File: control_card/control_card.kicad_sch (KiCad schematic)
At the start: 1 part, among them J1 Conn_02x04_Counter_Clockwise

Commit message: Control Card Started : Schematic & PCB
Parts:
- added C1, C5, C7: 0.1µF, Capacitor_SMD:C_0402_1005Metric, symbol Device:C_Small
- added C10, C11, C12, C13, C20, C3, C4, C6, C9: 1µF, Capacitor_SMD:C_0402_1005Metric, symbol Device:C_Small
- added C14: 18pF, Capacitor_SMD:C_0402_1005Metric, symbol Device:C_Small
- added C15: 2.7pF, Capacitor_SMD:C_0402_1005Metric, symbol Device:C_Small
- added C16: 220pF, Capacitor_SMD:C_0402_1005Metric, symbol Device:C_Small
- added C17: 2pF, Capacitor_SMD:C_0402_1005Metric, symbol Device:C_Small
- added C18: 0.5pF, Capacitor_SMD:C_0402_1005Metric, symbol Device:C_Small
- added C19: 1pF, Capacitor_SMD:C_0402_1005Metric, symbol Device:C_Small
- added C2: 10µF, Capacitor_SMD:C_0402_1005Metric, symbol Device:C_Small
- added C8: 2.2µF, Capacitor_SMD:C_0402_1005Metric, symbol Device:C_Small
- added IC1: TLSR8253F512ET48, Package_DFN_QFN:QFN-48-1EP_7x7mm_P0.5mm_EP5.6x5.6mm_ThermalVias, symbol Library:TLSR8253F512ET48
- added L1: 47µH, Inductor_SMD:L_0805_2012Metric, symbol Device:L_Small
- added L2: 1.3nH, Inductor_SMD:L_0402_1005Metric, symbol Device:L_Small
- added L3: 3.3nF, Inductor_SMD:L_0402_1005Metric, symbol Device:L_Small
- added U1: Wifi, Footprint_Rang_Dong:Wifi CBU, symbol Library:Wifi_CBU
- added Y1: Crystal_GND24_Small, Footprint_Rang_Dong:Crystal_SMD_3225, symbol Device:Crystal_GND24_Small
- J1: footprint Connector_PinSocket_2.54mm:PinSocket_2x04_P2.54mm_Vertical -> Connector_PinHeader_2.54mm:PinHeader_2x04_P2.54mm_Vertical
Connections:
- net +3.3V: now also C1.1, C10.1, C13.1, C2.1, C9.1, IC1.15 (VDD_IO), IC1.26 (VDD3), IC1.27 (VDDIO_AMS), U1.14 (3V3), U1.18 (CEN)
- net CT1: now also U1.10 (P6), U1.11 (P26), U1.8 (P8), U1.9 (P7)
- net GND: now also C1.2, C10.2, C11.2, C12.2, C13.2, C14.2, C15.2, C17.2, C18.2, C19.2, C2.2, C20.1, C3.2, C4.2, C5.2, C6.1, C7.1, C8.2, C9.2, IC1.12 (DVSS), IC1.14 (DVSS), IC1.49 (GND), U1.13 (GND), Y1.2, Y1.4
- new net: C16.2, C17.1, L3.1
- new net: IC1.17 (VDCDC), L1.1
- new net: IC1.16 (VDCDC_SW), L1.2
- new net +1V2: C5.1, C6.2, C7.2, C8.1, IC1.18 (VDD1V2), IC1.39 (AVDD1V2)
- new net ANT: C15.1, C16.1, IC1.38 (ANT), L2.1
- new net ANTENNA: C18.1, C19.1, L3.2
- new net Clock1: C11.1, IC1.40 (XC1), Y1.1
- new net Clock2: C12.1, IC1.41 (XC2), Y1.3
- new net In_1: IC1.34 (PC6), U1.1 (P14)
- new net In_2: IC1.33 (PC5), U1.2 (P16)
- new net In_3: IC1.32 (PC4), U1.3 (P20)
- new net In_4: IC1.31 (PC3), U1.4 (P22)
- new net Led_1: U1.17 (P28)
- new net Led_2: U1.19 (P9)
- new net Led_3: U1.20 (P17)
- new net Led_4: U1.21 (P15)
- new net Network_STT: U1.12 (P24)
- new net RST: C20.2, IC1.36 (RESETB)
- new net VANT: C14.1, IC1.37 (VANT), L2.2
- new net VDD1V: C3.1, IC1.13 (VDD1V)
- new net VDD_F: C4.1, IC1.19 (VDD_F)
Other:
- note added: "AVDD1V2"
- note added: "VDD1V2"
- note added: "VDD3"
- note added: "VDDIO"
- note added: "VDDIO_AMS"
- moved on the sheet: J1

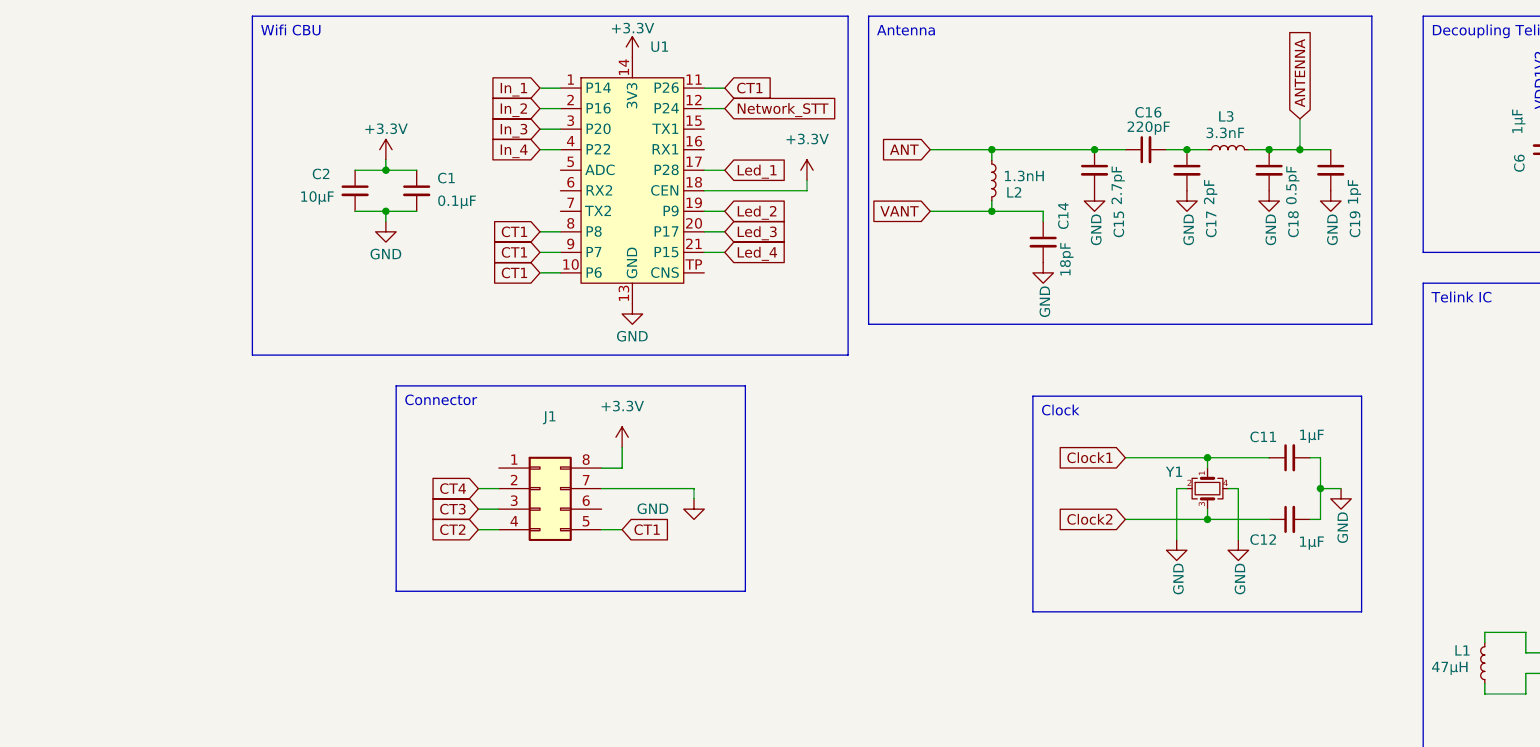
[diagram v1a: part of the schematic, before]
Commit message: PCB : started footprint and rooting
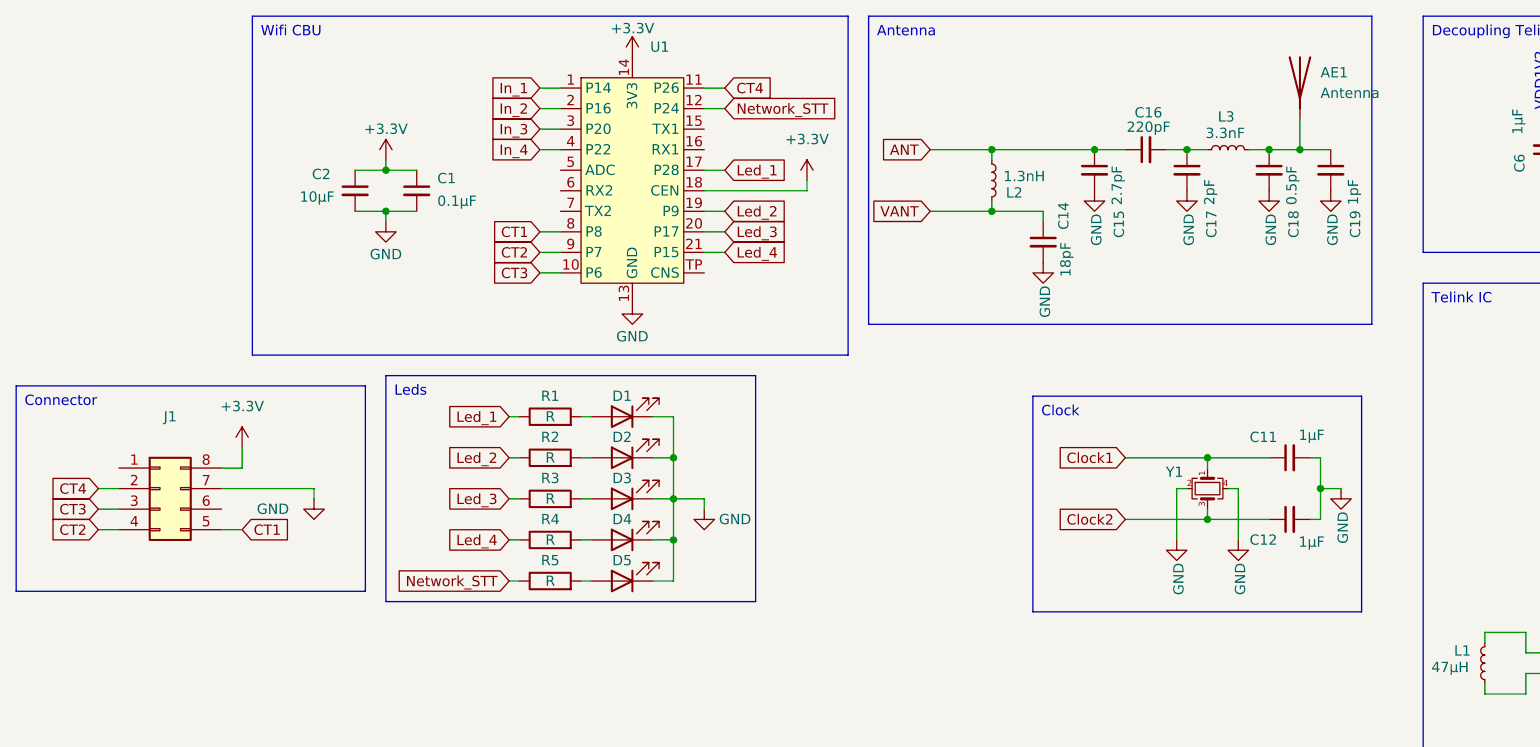
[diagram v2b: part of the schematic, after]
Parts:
- added AE1: Antenna, Footprint_Rang_Dong:Antenna, symbol Device:Antenna
- added D1, D2, D3, D4, D5: LED, LED_SMD:LED_0603_1608Metric, symbol Device:LED
- added R1, R2, R3, R4, R5: R, Resistor_SMD:R_0603_1608Metric, symbol Device:R
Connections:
- net CT1: no longer U1.10 (P6), U1.11 (P26), U1.9 (P7)
- net CT2: now also U1.9 (P7)
- net CT3: now also U1.10 (P6)
- net CT4: now also U1.11 (P26)
- net GND: now also D1.1 (K), D2.1 (K), D3.1 (K), D4.1 (K), D5.1 (K)
- net Led_1: now also R1.1
- net Led_2: now also R2.1
- net Led_3: now also R3.1
- net Led_4: now also R4.1
- net Network_STT: now also R5.1
- net ANTENNA: no longer names the net of C18.1, C19.1, L3.2
- net ANTENNA: now also AE1.1 (A)
- new net: D1.2 (A), R1.2
- new net: D2.2 (A), R2.2
- new net: D3.2 (A), R3.2
- new net: D4.2 (A), R4.2
- new net: D5.2 (A), R5.2
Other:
- moved on the sheet: J1

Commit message: PCB (control_card): Almost Finished
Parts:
- removed AE1: Antenna, Footprint_Rang_Dong:Antenna, symbol Device:Antenna
- added AE1: Antenna_Shield, Footprint_Rang_Dong:Antenna, symbol Device:Antenna_Shield
- D1, D2, D3, D4, D5: footprint LED_SMD:LED_0603_1608Metric -> LED_SMD:LED_0805_2012Metric
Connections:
- net GND: now also AE1.2 (Shield)
- net Led_1: now also R4.1; no longer R1.1
- net Led_2: now also R3.1; no longer R2.1
- net Led_3: now also R2.1; no longer R3.1
- net Led_4: now also R1.1; no longer R4.1
- net at C18.1, C19.1, L3.2: now also AE1.1 (A)
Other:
- moved on the sheet: D1, D2, D3, D4, D5, R1, R2, R3, R4, R5

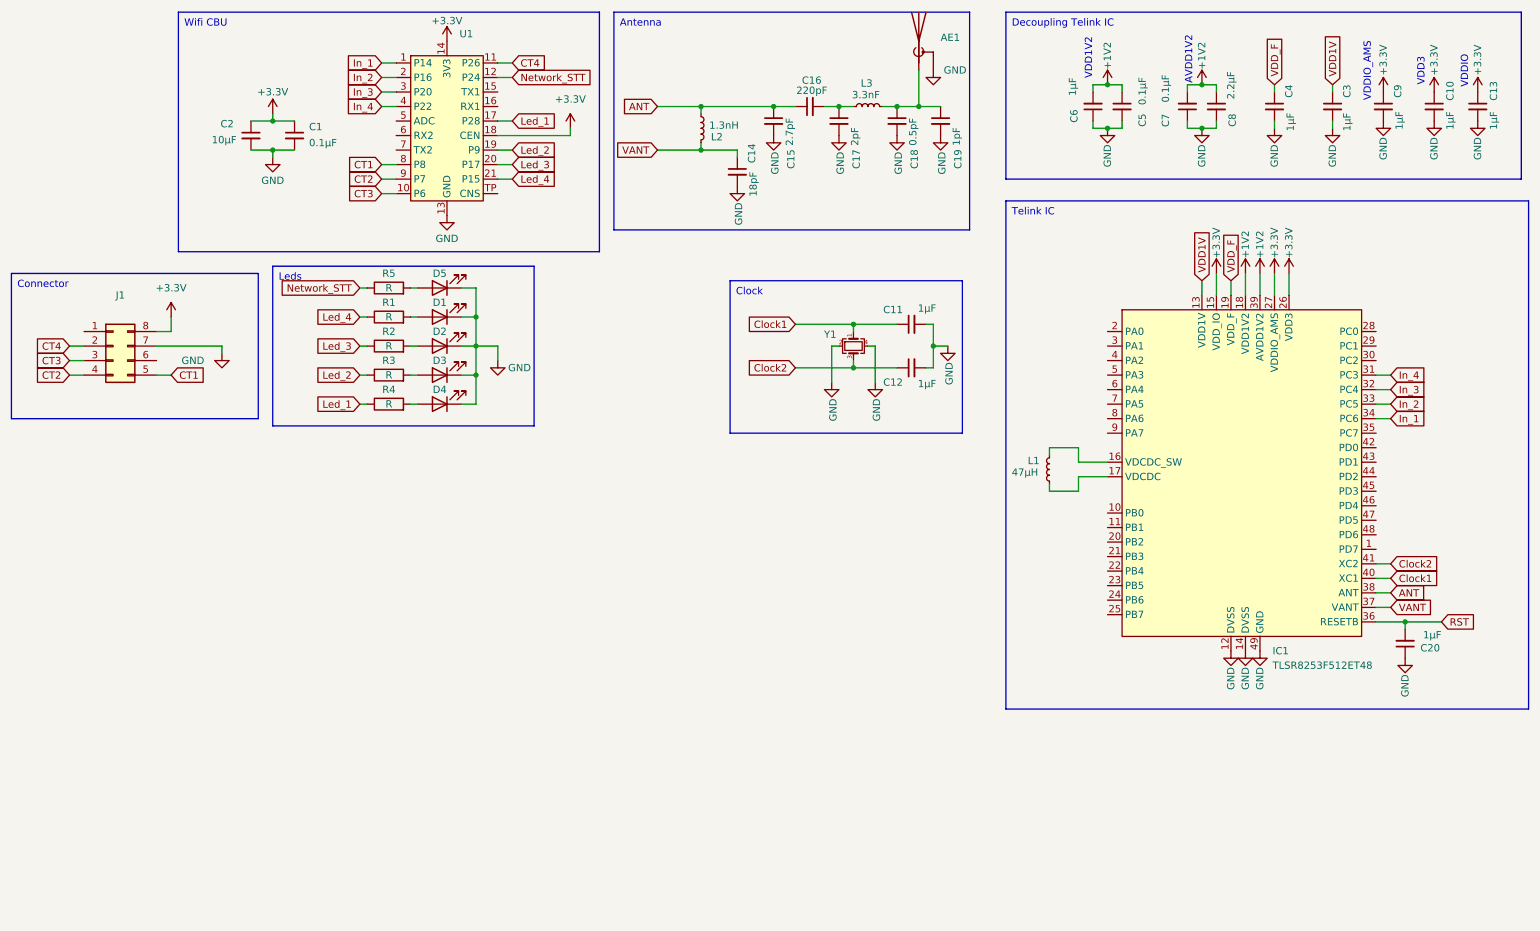
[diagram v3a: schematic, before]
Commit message: PCB (control_card): V2 almost finished
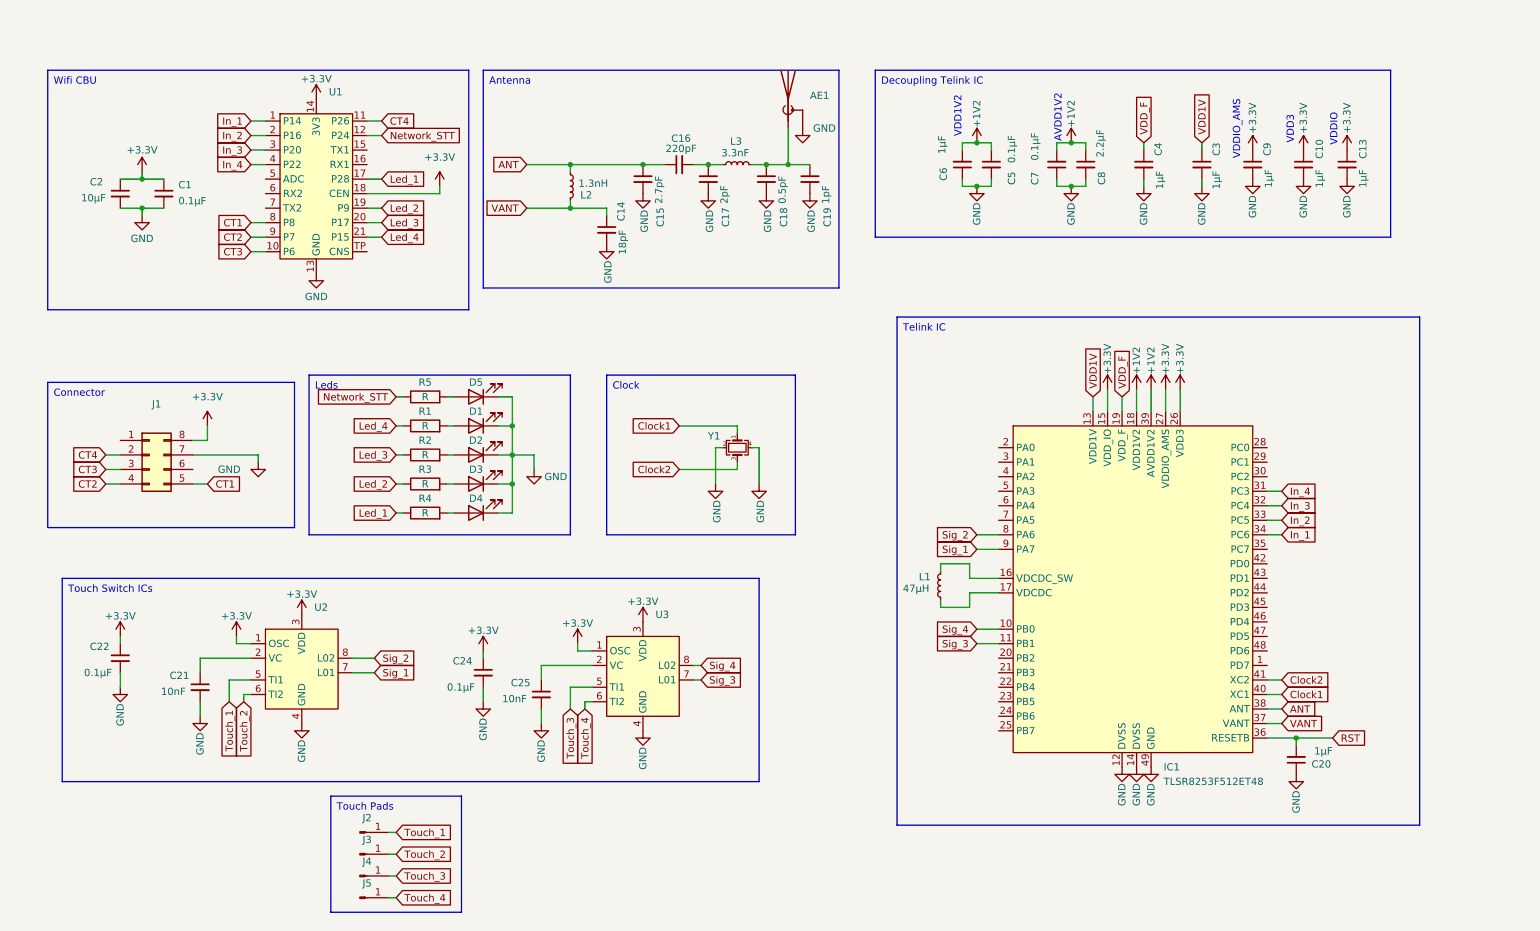
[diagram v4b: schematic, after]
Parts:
- removed C11, C12: 1µF, Capacitor_SMD:C_0402_1005Metric, symbol Device:C_Small
- added C21, C25: 10nF, Capacitor_SMD:C_0402_1005Metric, symbol Device:C_Small
- added C22, C24: 0.1µF, Capacitor_SMD:C_0402_1005Metric, symbol Device:C_Small
- added J2, J3, J4, J5: Conn_01x01_Pin, Footprint_Rang_Dong:Touch-Pad, symbol Connector:Conn_01x01_Pin
- added U2, U3: ~, Package_SO:SOIC-8_3.9x4.9mm_P1.27mm, symbol Library:SGL8022K
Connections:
- net +3.3V: now also C22.1, C24.1, U2.1 (OSC), U2.3 (VDD), U3.1 (OSC), U3.3 (VDD)
- net GND: now also C21.2, C22.2, C24.2, C25.2, U2.4 (GND), U3.4 (GND)
- net Sig_4: now reaches IC1.10 (PB0)
- net Sig_4: now also U3.8 (L02)
- net Sig_3: now reaches IC1.11 (PB1)
- net Sig_3: now also U3.7 (L01)
- net Sig_2: now reaches IC1.8 (PA6)
- net Sig_2: now also U2.8 (L02)
- net Sig_1: now reaches IC1.9 (PA7)
- net Sig_1: now also U2.7 (L01)
- new net: C25.1, U3.2 (VC)
- new net: C21.1, U2.2 (VC)
- new net Touch_1: J2.1 (Pin_1), U2.5 (TI1)
- new net Touch_2: J3.1 (Pin_1), U2.6 (TI2)
- new net Touch_3: J4.1 (Pin_1), U3.5 (TI1)
- new net Touch_4: J5.1 (Pin_1), U3.6 (TI2)
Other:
- moved on the sheet: AE1, C1, C10, C13, C14, C15, C16, C17, C18, C19, C2, C20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

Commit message: PCB (control_card) : V3 finished, perfect dimension
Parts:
- C1, C10, C13, C14, C15, C16, C17, C18, C19, C2, C20, C21, C22, C24, C25, C3, C4, C5, C6, C7, C8, C9: footprint Capacitor_SMD:C_0402_1005Metric -> Capacitor_SMD:C_0603_1608Metric
- J1: footprint Connector_PinHeader_2.54mm:PinHeader_2x04_P2.54mm_Vertical -> Footprint_Rang_Dong:Male connector
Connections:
- net Touch_1: now also J4.1 (Pin_1); no longer J2.1 (Pin_1)
- net Touch_2: now also J2.1 (Pin_1); no longer J3.1 (Pin_1)
- net Touch_3: now also J5.1 (Pin_1); no longer J4.1 (Pin_1)
- net Touch_4: now also J3.1 (Pin_1); no longer J5.1 (Pin_1)
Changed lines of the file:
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@@
 		)
 	)
-	(global_label "Touch_2"
+	(global_label "Touch_4"
 		(shape input)
 		(at 86.36 161.29 0)
@@
 		)
 	)
-	(global_label "Touch_3"
+	(global_label "Touch_1"
 		(shape input)
 		(at 86.36 165.1 0)
@@
 		)
 	)
-	(global_label "Touch_1"
+	(global_label "Touch_2"
 		(shape input)
 		(at 86.36 157.48 0)
@@
 		)
 	)
-	(global_label "Touch_4"
+	(global_label "Touch_3"
 		(shape input)
 		(at 86.36 168.91 0)
@@
 			)
 		)
-		(property "Footprint" "Capacitor_SMD:C_0402_1005Metric"
+		(property "Footprint" "Capacitor_SMD:C_0603_1608Metric"
 			(at 135.89 40.64 0)
 			(effects
@@
 			)
 		)
-		(property "Footprint" "Capacitor_SMD:C_0402_1005Metric"
+		(property "Footprint" "Capacitor_SMD:C_0603_1608Metric"
 			(at 140.97 43.18 0)
 			(effects
@@
 			)
 		)
-		(property "Footprint" "Capacitor_SMD:C_0402_1005Metric"
+		(property "Footprint" "Capacitor_SMD:C_0603_1608Metric"
 			(at 101.6 129.54 0)
 			(effects
@@
 			)
 		)
-		(property "Footprint" "Capacitor_SMD:C_0402_1005Metric"
+		(property "Footprint" "Capacitor_SMD:C_0603_1608Metric"
 			(at 190.5 40.64 0)
 			(effects
@@
 			)
 		)
-		(property "Footprint" "Capacitor_SMD:C_0402_1005Metric"
+		(property "Footprint" "Capacitor_SMD:C_0603_1608Metric"
 			(at 217.17 40.64 0)
 			(effects
@@
 			)
 		)
-		(property "Footprint" "Capacitor_SMD:C_0402_1005Metric"
+		(property "Footprint" "Capacitor_SMD:C_0603_1608Metric"
 			(at 129.54 43.18 0)
 			(effects
@@
 			)
 		)
-		(property "Footprint" "Capacitor_SMD:C_0402_1005Metric"
+		(property "Footprint" "Capacitor_SMD:C_0603_1608Metric"
 			(at 201.93 40.64 0)
 			(effects
@@
 			)
 		)
-		(property "Footprint" "Capacitor_SMD:C_0402_1005Metric"
+		(property "Footprint" "Capacitor_SMD:C_0603_1608Metric"
 			(at 45.72 45.72 0)
 			(effects
@@
 			)
 		)
-		(property "Footprint" "Capacitor_SMD:C_0402_1005Metric"
+		(property "Footprint" "Capacitor_SMD:C_0603_1608Metric"
 			(at 38.1 127 0)
 			(effects
@@
 			)
 		)
-		(property "Footprint" "Capacitor_SMD:C_0402_1005Metric"
+		(property "Footprint" "Capacitor_SMD:C_0603_1608Metric"
 			(at 236.22 40.64 0)
 			(effects
@@
 			)
 		)
-		(property "Footprint" "Capacitor_SMD:C_0402_1005Metric"
+		(property "Footprint" "Capacitor_SMD:C_0603_1608Metric"
 			(at 151.13 43.18 0)
 			(effects
@@
 			)
 		)
-		(property "Footprint" "Capacitor_SMD:C_0402_1005Metric"
+		(property "Footprint" "Capacitor_SMD:C_0603_1608Metric"
 			(at 52.07 132.08 0)
 			(effects
@@
 			)
 		)
-		(property "Footprint" "Capacitor_SMD:C_0402_1005Metric"
+		(property "Footprint" "Capacitor_SMD:C_0603_1608Metric"
 			(at 123.19 52.07 0)
 			(effects
@@
 			)
 		)
-		(property "Footprint" "Capacitor_SMD:C_0402_1005Metric"
+		(property "Footprint" "Capacitor_SMD:C_0603_1608Metric"
 			(at 245.11 40.64 0)
 			(effects
@@
 			)
 		)
-		(property "Footprint" "Capacitor_SMD:C_0402_1005Metric"
+		(property "Footprint" "Capacitor_SMD:C_0603_1608Metric"
 			(at 185.42 40.64 0)
 			(effects
@@
 			)
 		)
-		(property "Footprint" "Capacitor_SMD:C_0402_1005Metric"
+		(property "Footprint" "Capacitor_SMD:C_0603_1608Metric"
 			(at 243.84 144.78 0)
 			(effects
@@
 			)
 		)
-		(property "Footprint" "Connector_PinHeader_2.54mm:PinHeader_2x04_P2.54mm_Vertical"
+		(property "Footprint" "Footprint_Rang_Dong:Male connector"
 			(at 43.18 91.44 0)
 			(effects
@@
 			)
 		)
-		(property "Footprint" "Capacitor_SMD:C_0402_1005Metric"
+		(property "Footprint" "Capacitor_SMD:C_0603_1608Metric"
 			(at 207.01 40.64 0)
 			(effects
@@
 			)
 		)
-		(property "Footprint" "Capacitor_SMD:C_0402_1005Metric"
+		(property "Footprint" "Capacitor_SMD:C_0603_1608Metric"
 			(at 252.73 40.64 0)
 			(effects
@@
 			)
 		)
-		(property "Footprint" "Capacitor_SMD:C_0402_1005Metric"
+		(property "Footprint" "Capacitor_SMD:C_0603_1608Metric"
 			(at 227.33 40.64 0)
 			(effects
@@
 			)
 		)
-		(property "Footprint" "Capacitor_SMD:C_0402_1005Metric"
+		(property "Footprint" "Capacitor_SMD:C_0603_1608Metric"
 			(at 111.76 133.35 0)
 			(effects
@@
 			)
 		)
-		(property "Footprint" "Capacitor_SMD:C_0402_1005Metric"
+		(property "Footprint" "Capacitor_SMD:C_0603_1608Metric"
 			(at 158.75 43.18 0)
 			(effects
@@
 			)
 		)
-		(property "Footprint" "Capacitor_SMD:C_0402_1005Metric"
+		(property "Footprint" "Capacitor_SMD:C_0603_1608Metric"
 			(at 38.1 45.72 0)
 			(effects
